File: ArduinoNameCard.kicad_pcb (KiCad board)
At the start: 2 copper layers, 91 x 55 mm, 29 parts, among them J1 USB_B_Micro, J2 Conn_01x04, J3 Conn_01x06, J4 Conn_01x08, J5 Conn_01x06, SW1 SW_Push

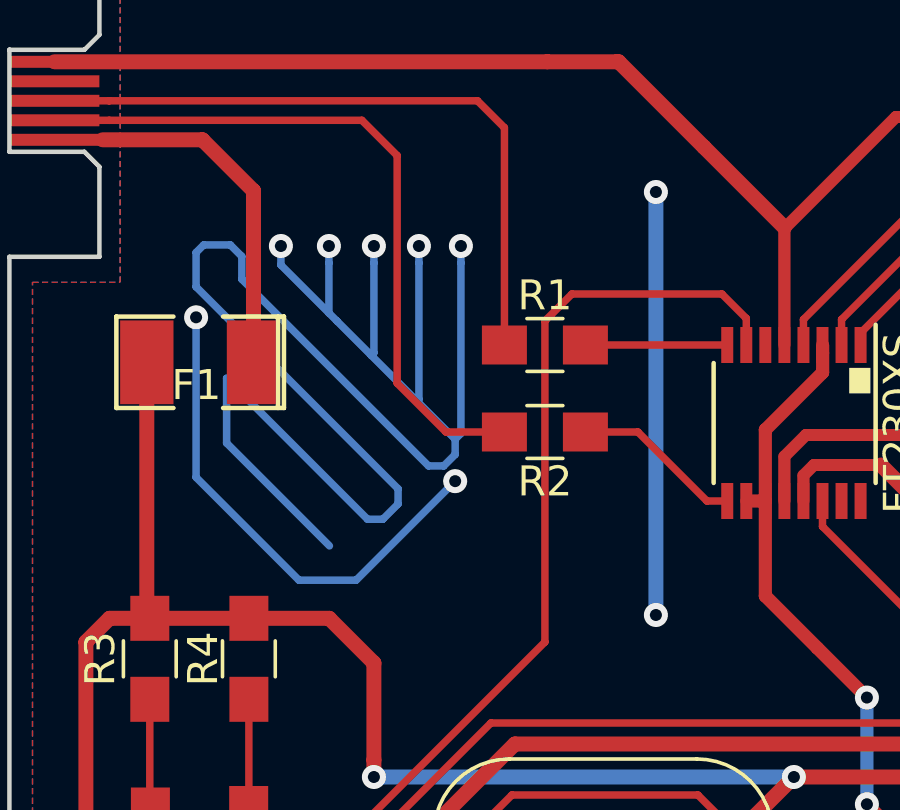
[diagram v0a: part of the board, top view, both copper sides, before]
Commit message: githubのQRコードを追加した。
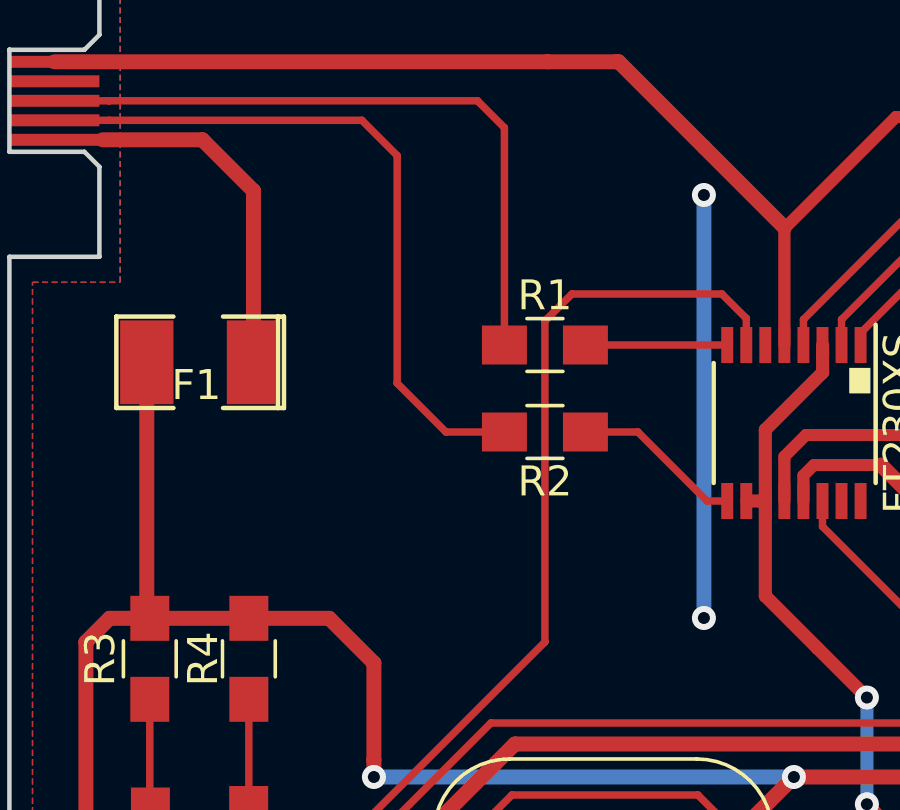
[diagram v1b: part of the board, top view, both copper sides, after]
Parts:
- added G***: LOGO, ArduinoNameCard:qr_github, B.Cu at (108.7, 76.2)
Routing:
- net (no net): track 96.4 -> 14.1 mm, vias 9 -> 2
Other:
- board text added: "github"
